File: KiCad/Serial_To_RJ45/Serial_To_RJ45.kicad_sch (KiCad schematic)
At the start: 2 parts, among them J1 RJE561881410, J2 Serial IDC Header

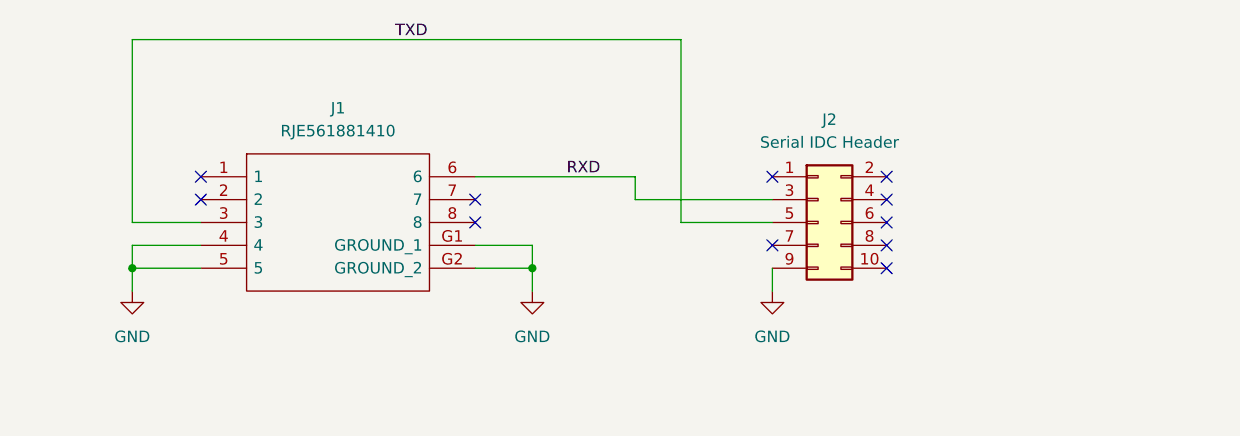
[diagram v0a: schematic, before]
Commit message: Added Switch for RX TX
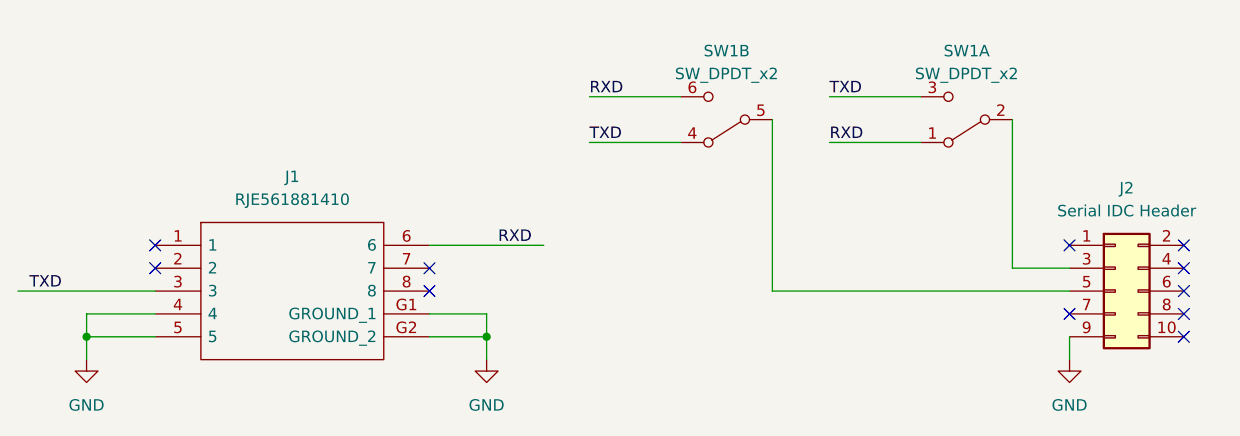
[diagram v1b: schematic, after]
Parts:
- added SW1: SW_DPDT_x2, Button_Switch_THT:SW_CuK_JS202011CQN_DPDT_Straight, symbol Switch:SW_DPDT_x2
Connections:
- net RXD: now also SW1.1 (A), SW1.6 (C); no longer J2.3 (Pin_3)
- net TXD: now also SW1.3 (C), SW1.4 (A); no longer J2.5 (Pin_5)
- new net: J2.3 (Pin_3), SW1.2 (B)
- new net: J2.5 (Pin_5), SW1.5 (B)
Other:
- moved on the sheet: J1, J2
